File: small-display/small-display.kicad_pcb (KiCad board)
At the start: 4 copper layers, 43 x 62 mm, 44 parts, among them J1 2047110001, J2 Micro_SD_Card_Det, J5 F32D-1A7Y1-21040, U1 TPD4EUSB30, U2 74LVC1G07SE-7, U3 RT9742GGJ5, U4 PAM2804AAB010, U5 USB2412-DZK, U6 NLVVHC1G04DFT1G, U7 M24M01-DFDW6TP, Y1 ECS-240-8-33-AGN-TR

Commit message: Routing the board.
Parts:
- R6, R7, U1: moved to F.Cu
- moved TP3 72.0 mm to (22.5, 65.5)
- moved U1 62.4 mm to (28.5, 56.8), turned to -90 degrees
- moved R6 62.3 mm to (28.0, 59.0), turned to 90 degrees
- moved TP4 61.9 mm to (11.0, 13.8)
- moved C3 61.1 mm to (-37.2, 47.8)
- moved U6 59.0 mm to (7.72, 13.2)
- moved R5 58.0 mm to (-40.2, 44.8)
- moved R4 57.2 mm to (-34.5, 43.0)
- moved TP6 56.6 mm to (11.0, 16.2)
- moved C4 54.6 mm to (4.25, 13.5)
- moved R2 53.7 mm to (-38.5, 29.2)
- moved Y1 51.0 mm to (6.40, 23.5), turned to 0 degrees
- moved U4 50.0 mm to (-32.0, 46.5)
- moved R7 48.5 mm to (15.0, 58.5), turned to 90 degrees
- moved C5 46.4 mm to (3.25, 23.3), turned to -90 degrees
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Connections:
- net /CAM1_C_N renamed CAM1_C_N
- net /CAM1_C_P renamed CAM1_C_P
- net /CAM1_D0_N renamed CAM1_D0_N
- net /CAM1_D0_P renamed CAM1_D0_P
- net /CAM1_D1_N renamed CAM1_D1_N
- net /CAM1_D1_P renamed CAM1_D1_P
- net /CAM1_D2_N renamed CAM1_D2_N
- net /CAM1_D2_P renamed CAM1_D2_P
- net /CAM1_D3_N renamed CAM1_D3_N
- net /CAM1_D3_P renamed CAM1_D3_P
- net /DSI0_C_N renamed DSI0_C_N
- net /DSI0_C_P renamed DSI0_C_P
- net /DSI0_D0_N renamed DSI0_D0_N
- net /DSI0_D0_P renamed DSI0_D0_P
- net /DSI0_D1_N renamed DSI0_D1_N
- net /DSI0_D1_P renamed DSI0_D1_P
- net /DSI1_C_N renamed DSI1_C_N
- net /DSI1_C_P renamed DSI1_C_P
- net /DSI1_D0_N renamed DSI1_D0_N
- net /DSI1_D0_P renamed DSI1_D0_P
- net /DSI1_D1_N renamed DSI1_D1_N
- net /DSI1_D1_P renamed DSI1_D1_P
- net /DSI1_D2_N renamed DSI1_D2_N
- net /DSI1_D2_P renamed DSI1_D2_P
- net /GLOBAL_EN renamed GLOBAL_EN
- net /HDMI0_CEC renamed HDMI0_CEC
- net /HDMI0_HOTPLUG renamed HDMI0_HOTPLUG
- net /HDMI0_SDA renamed HDMI0_SDA
- net /HDMI1_CEC renamed HDMI1_CEC
- net /HDMI1_HOTPLUG renamed HDMI1_HOTPLUG
- net /HDMI1_SCL renamed HDMI1_SCL
- net /HDMI1_SDA renamed HDMI1_SDA
- net /PCIE_nRST renamed PCIE_nRST
- net /TV_OUT renamed TV_OUT
- net GPIO_VREF renamed +3.3v
- C1 pad 2: TRD1_N -> GND
- C2 pad 2: TRD1_N -> GND
- C3 pad 2: TRD1_N -> GND
- C4 pad 2: TRD1_N -> GND
- C5 pad 2: TRD1_N -> GND
- C6 pad 2: TRD1_N -> GND
- CX1 pad 2: TRD1_N -> GND
- CX2 pad 2: TRD1_N -> GND
- J1 pad A1: TRD1_N -> GND
- J1 pad A12: TRD1_N -> GND
- J1 pad B1: TRD1_N -> GND
- J1 pad B12: TRD1_N -> GND
- J1 pad S1: TRD1_N -> GND
- J1 pad S2: TRD1_N -> GND
- J1 pad S3: TRD1_N -> GND
- J1 pad S4: TRD1_N -> GND
- J1 pad S5: TRD1_N -> GND
- J1 pad S6: TRD1_N -> GND
- J2 pad 11: TRD1_N -> GND
- J2 pad 6: TRD1_N -> GND
- J5 pad 1: TRD1_N -> GND
- J5 pad 10: TRD1_N -> GND
- J5 pad 31: TRD1_N -> GND
- J5 pad 33: TRD1_N -> GND
- J5 pad 39: TRD1_N -> GND
- Module1 pad 1: TRD1_N -> GND
- Module1 pad 10: TRD1_N -> unconnected-(Module1-Pad10)
- Module1 pad 107: TRD1_N -> GND
- Module1 pad 108: TRD1_N -> GND
- Module1 pad 113: TRD1_N -> GND
- Module1 pad 114: TRD1_N -> GND
- Module1 pad 119: TRD1_N -> GND
- Module1 pad 12: TRD0_P -> unconnected-(Module1-Pad12)
- Module1 pad 120: TRD1_N -> GND
- Module1 pad 125: TRD1_N -> GND
- Module1 pad 126: TRD1_N -> GND
- Module1 pad 13: TRD1_N -> GND
- Module1 pad 131: TRD1_N -> GND
- Module1 pad 132: TRD1_N -> GND
- Module1 pad 137: TRD1_N -> GND
- Module1 pad 138: TRD1_N -> GND
- Module1 pad 14: TRD1_N -> GND
- Module1 pad 144: TRD1_N -> GND
- Module1 pad 150: TRD1_N -> GND
- Module1 pad 155: TRD1_N -> GND
- Module1 pad 156: TRD1_N -> GND
- Module1 pad 16: TRD1_N -> unconnected-(Module1-Pad16)
- Module1 pad 161: TRD1_N -> GND
- Module1 pad 162: TRD1_N -> GND
- Module1 pad 167: TRD1_N -> GND
- Module1 pad 168: TRD1_N -> GND
- Module1 pad 173: TRD1_N -> GND
- Module1 pad 174: TRD1_N -> GND
- Module1 pad 179: TRD1_N -> GND
- Module1 pad 18: TRD1_N -> unconnected-(Module1-Pad18)
- Module1 pad 180: TRD1_N -> GND
- Module1 pad 185: TRD1_N -> GND
- Module1 pad 186: TRD1_N -> GND
- Module1 pad 191: TRD1_N -> GND
- Module1 pad 192: TRD1_N -> GND
- Module1 pad 197: TRD1_N -> GND
- Module1 pad 198: TRD1_N -> GND
- Module1 pad 2: TRD1_N -> GND
- Module1 pad 20: TRD1_N -> unconnected-(Module1-Pad20)
- Module1 pad 22: TRD1_N -> GND
- Module1 pad 23: TRD1_N -> GND
- Module1 pad 32: TRD1_N -> GND
- Module1 pad 33: TRD1_N -> GND
- Module1 pad 4: TRD1_N -> unconnected-(Module1-Pad4)
- Module1 pad 42: TRD1_N -> GND
- Module1 pad 43: TRD1_N -> GND
- Module1 pad 52: TRD1_N -> GND
- Module1 pad 53: TRD1_N -> GND
- Module1 pad 59: TRD1_N -> GND
- Module1 pad 6: TRD1_N -> unconnected-(Module1-Pad6)
- Module1 pad 60: TRD1_N -> GND
- Module1 pad 65: TRD1_N -> GND
- Module1 pad 66: TRD1_N -> GND
- Module1 pad 7: TRD1_N -> GND
- Module1 pad 71: TRD1_N -> GND
- Module1 pad 74: TRD1_N -> GND
- Module1 pad 8: TRD1_N -> GND
- Module1 pad 98: TRD1_N -> GND
- R4 pad 2: TRD1_N -> GND
- R5 pad 2: TRD1_N -> GND
- R6 pad 1: TRD1_N -> GND
- R7 pad 1: TRD1_N -> GND
- R9 pad 2: TRD1_N -> GND
- U1 pad 3: TRD1_N -> GND
- U1 pad 8: TRD1_N -> GND
- U2 pad 3: TRD1_N -> GND
- U3 pad 2: TRD1_N -> GND
- U4 pad 2: TRD1_N -> GND
- U5 pad 13: TRD1_N -> GND
- U5 pad 15: TRD1_N -> GND
- U5 pad 19: TRD1_N -> GND
- U5 pad 29: TRD1_N -> GND
- U6 pad 3: TRD1_N -> GND
- U7 pad 2: TRD1_N -> GND
- U7 pad 3: TRD1_N -> GND
- U7 pad 4: TRD1_N -> GND
- U7 pad 7: TRD1_N -> GND
- Y1 pad 2: TRD1_N -> GND
- Y1 pad 4: TRD1_N -> GND
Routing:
- net USBD_P: track 2.82 -> 59.2 mm
- net USBD_N: track 5.90 -> 61.6 mm
- net GPIO_02_USB_!RESET: track 0.00 -> 39.5 mm, vias 0 -> 2
- net USB2_P: track 0.93 -> 21.7 mm
- net USB2_N: track 0.87 -> 21.4 mm
- net Net-(CX2-Pad1): track 0.00 -> 10.1 mm
- net Net-(CX1-Pad1): track 0.00 -> 9.97 mm
- net Net-(J1-PadB5): track 0.00 -> 8.77 mm, vias 0 -> 2
- net Net-(R9-Pad1): track 0.00 -> 8.38 mm
- net Net-(J1-PadA5): track 0.00 -> 7.85 mm, vias 0 -> 2
- net Net-(TP6-Pad1): track 0.00 -> 7.83 mm
- net +3.3V: track 0.00 -> 6.44 mm, vias 0 -> 6
- net Net-(C5-Pad1): track 0.00 -> 3.82 mm
- net (no net): track 3.02 -> 0.00 mm
- net +5V: track 0.25 -> 2.98 mm, vias 0 -> 4
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- added copper zone on B.Cu, net GND
- added copper zone on F.Cu, net GND
- removed copper zone on B.Cu, net TRD1_N
- removed copper zone on F.Cu, net TRD1_N
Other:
- board text added: "I2C memory"
- board text added: "LCD panel backlight driver"
- board text added: "LED indicators (move to front)"
- board text added: "SD card power"

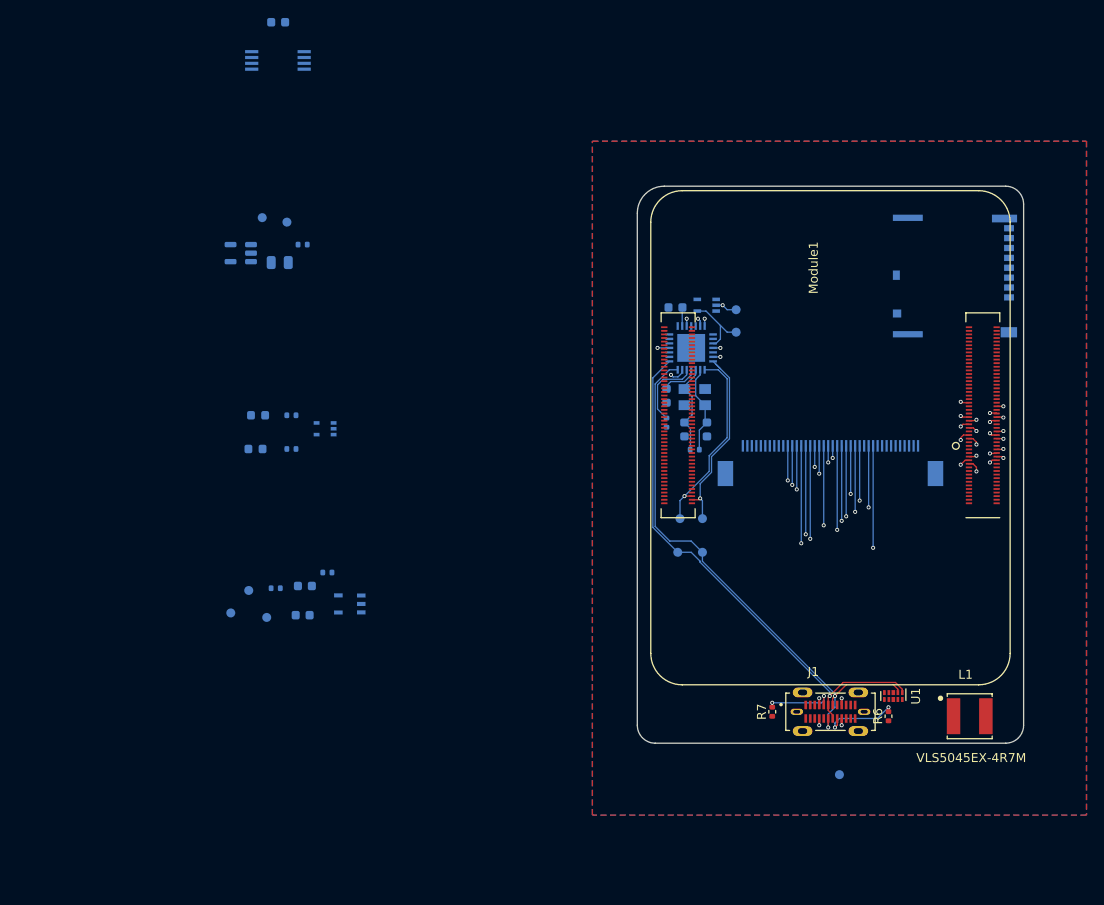
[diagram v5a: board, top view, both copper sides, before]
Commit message: More routing of small-display.
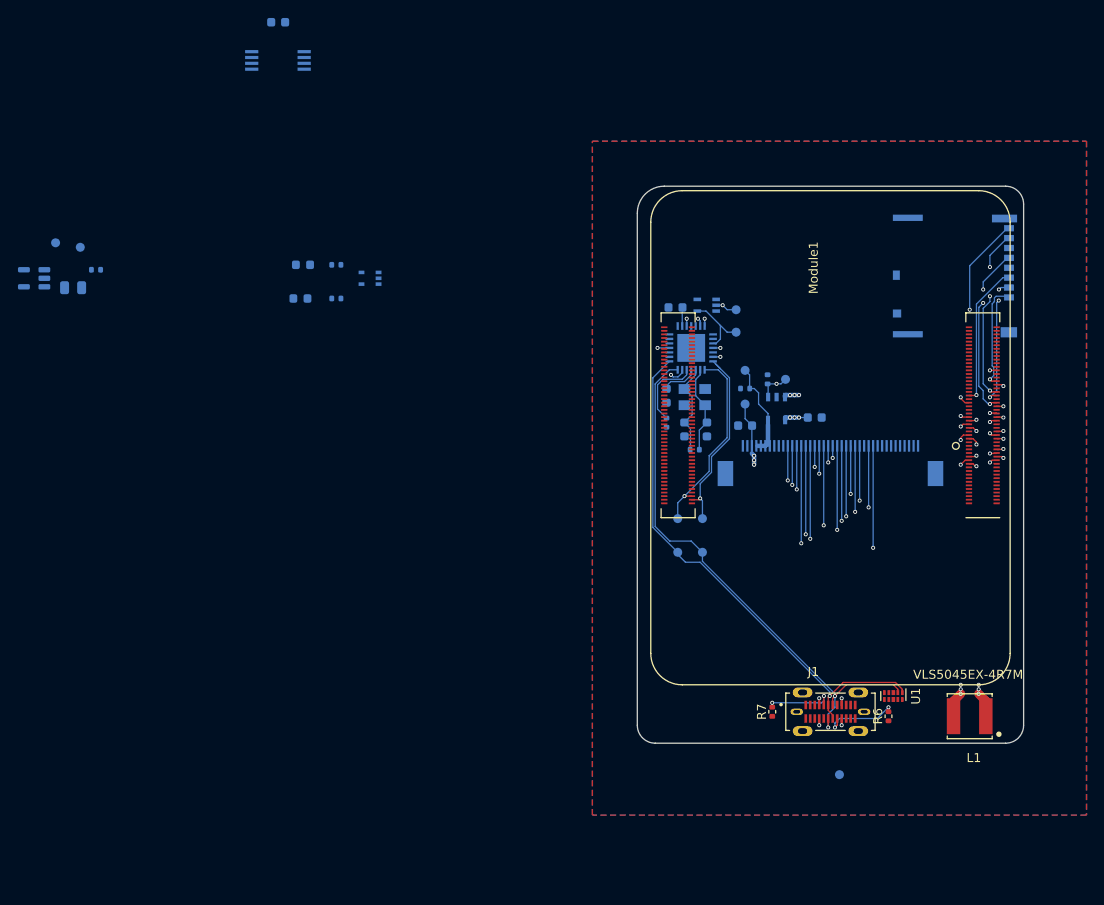
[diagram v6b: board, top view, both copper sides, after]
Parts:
- moved TP2 63.5 mm to (16.5, 21.5)
- moved TP7 61.8 mm to (12.0, 24.2)
- moved TP8 60.4 mm to (12.0, 20.5)
- moved C2 59.8 mm to (19.8, 25.8), turned to 0 degrees
- moved R5 56.8 mm to (12.0, 22.5)
- moved C3 53.6 mm to (12.0, 26.6)
- moved R4 53.5 mm to (14.5, 21.5), turned to 90 degrees
- moved U4 52.2 mm to (15.5, 24.8), turned to -90 degrees
- moved C1 23.2 mm to (-62.8, 11.3)
- moved R3 23.2 mm to (-60.2, 9.30)
- moved TP1 23.2 mm to (-62.0, 6.80)
- moved TP5 23.2 mm to (-64.8, 6.30)
- moved U3 23.2 mm to (-67.1, 10.2)
- moved D1 17.5 mm to (-37.2, 8.75)
- moved D2 17.5 mm to (-37.5, 12.5)
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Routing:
- net Net-(L1-Pad1): track 0.00 -> 54.6 mm, vias 0 -> 6
- net /LED_A: track 0.00 -> 49.3 mm, vias 0 -> 6
- net GPIO_25_PWM: track 0.77 -> 34.4 mm, vias 1 -> 2
- net SD_DAT1: track 0.00 -> 21.9 mm, vias 0 -> 2
- net SD_DAT0: track 0.00 -> 19.4 mm, vias 0 -> 3
- net SD_CLK: track 0.00 -> 19.2 mm, vias 0 -> 3
- net SD_CMD: track 0.00 -> 15.8 mm, vias 0 -> 1
- net SD_DAT3: track 0.00 -> 14.5 mm, vias 0 -> 3
- net SD_DAT2: track 0.00 -> 12.2 mm, vias 0 -> 1
- net /LED_K: track 0.00 -> 11.7 mm
- net GPIO_02_USB_!RESET: track 39.5 -> 34.4 mm
- net +5V: track 2.98 -> 5.75 mm, vias 4 -> 7
- net SD_PWR_ON: track 0.00 -> 0.75 mm, vias 0 -> 1
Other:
- board text removed: "LCD panel backlight driver"

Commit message: First complete routing done.
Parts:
- D1, D2, R1, R2, U2: moved to F.Cu
- moved U3 90.9 mm to (23.8, 11.0)
- moved C1 90.1 mm to (27.2, 11.0), turned to -90 degrees
- moved TP1 88.0 mm to (26.0, 8.25)
- moved TP5 85.8 mm to (20.8, 13.2)
- moved C6 84.0 mm to (33.2, 23.0)
- moved R3 81.3 mm to (21.0, 11.0), turned to -90 degrees
- moved U7 78.6 mm to (30.8, 20.2), turned to 0 degrees
- moved D2 68.5 mm to (11.8, 60.0), turned to -90 degrees
- moved D1 67.2 mm to (6.27, 60.0), turned to -90 degrees
- moved R2 63.7 mm to (11.8, 57.3), turned to 90 degrees
- moved R1 62.7 mm to (6.27, 57.3), turned to 90 degrees
- moved U2 61.2 mm to (8.77, 57.8), turned to 0 degrees
- moved TP3 12.1 mm to (31.8, 57.8)
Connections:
- net +1.8v renamed +1.8V
- D1 pad 2: +3.3v -> +3.3V
- D2 pad 2: +3.3v -> +3.3V
- Module1 pad 78: +3.3v -> +3.3V
- Module1 pad 84: +3.3v -> +3.3V
- Module1 pad 86: +3.3v -> +3.3V
- Module1 pad 95: unconnected-(Module1-Pad95) -> nPWR_LED
- R3 pad 1: +3.3v -> +3.3V
- U2 pad 2: /nPWR_LED -> nPWR_LED
- U2 pad 5: +3.3v -> +3.3V
- U3 pad 5: +3.3v -> +3.3V
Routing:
- net nPWR_LED: track 0.00 -> 63.1 mm, vias 0 -> 2
- net PI_nLED_Activity: track 0.00 -> 45.8 mm, vias 0 -> 2
- net SD_PWR_ON: track 0.75 -> 25.0 mm, vias 1 -> 2
- net /SD_PWR: track 0.00 -> 19.4 mm, vias 0 -> 2
- net +5V: track 5.75 -> 21.0 mm, vias 7 -> 14
- net +3.3V: track 6.44 -> 21.0 mm, vias 6 -> 18
- net SD_CLK: track 19.2 -> 23.1 mm
- net SCL0: track 0.00 -> 3.34 mm, vias 0 -> 1
- net SDA0: track 0.00 -> 3.28 mm, vias 0 -> 1
- net Net-(R2-Pad2): track 0.00 -> 2.72 mm
- net SD_DAT1: track 21.9 -> 23.6 mm
- net Net-(D2-Pad1): track 0.00 -> 1.46 mm
- net Net-(D1-Pad1): track 0.00 -> 1.45 mm
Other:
- board text removed: "SD card power"

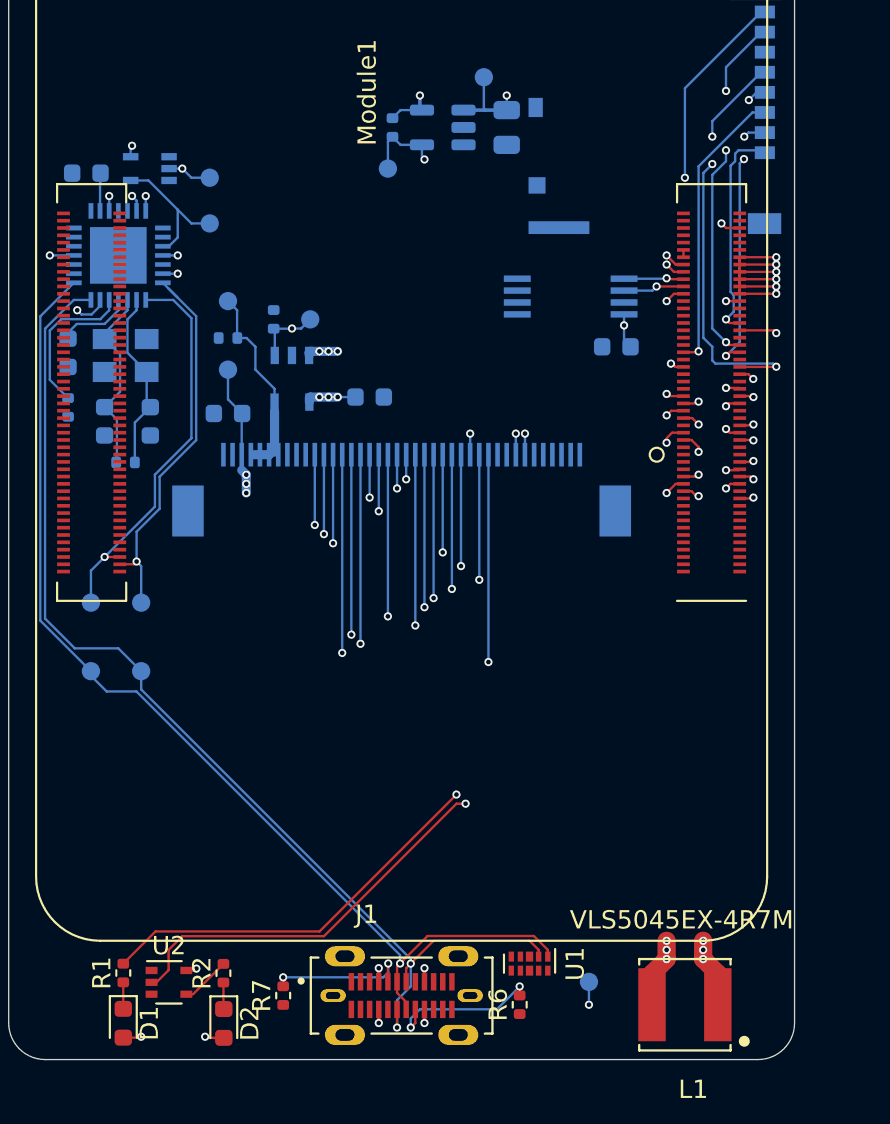
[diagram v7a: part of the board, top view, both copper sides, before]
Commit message: More routing refinements.
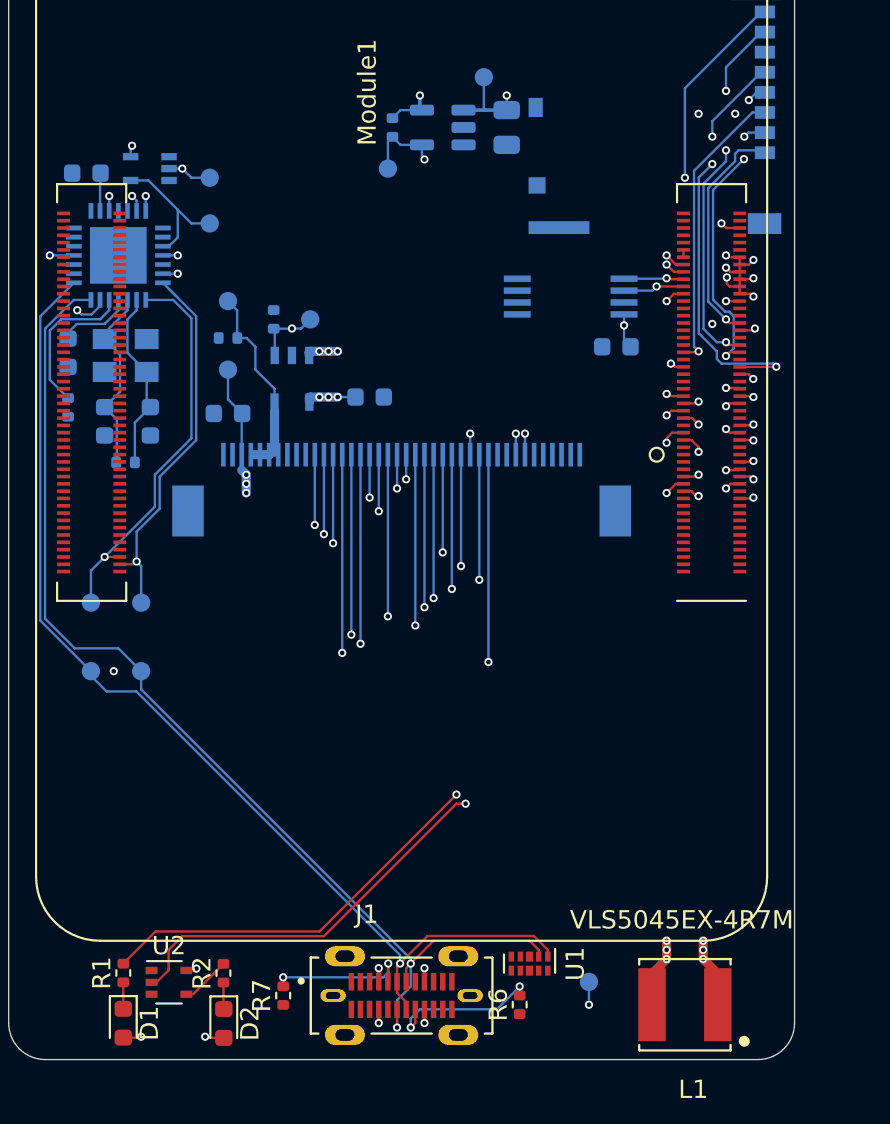
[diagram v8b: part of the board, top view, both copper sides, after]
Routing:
- net +5V: track 21.0 -> 14.2 mm
- net SD_DAT1: track 23.6 -> 21.7 mm
- net SD_DAT3: track 14.5 -> 15.5 mm
- net nPWR_LED: track 63.1 -> 63.9 mm
- net SD_DAT0: track 19.4 -> 20.1 mm
- net SD_DAT2: track 12.2 -> 12.9 mm
- net GND: vias 1 -> 5
